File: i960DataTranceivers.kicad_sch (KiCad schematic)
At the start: 6 parts

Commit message: Update everything and keep laying out the i960 features
Use bus wires as much as possible
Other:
- company: (none) -> Joshua Scoggins
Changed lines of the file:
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@@
 (kicad_sch (version 20211123) (generator eeschema)
   (paper "A4")
+  (title_block
+    (date "2022-05-13")
+    (rev "1")
+    (company "Joshua Scoggins")
+  )
   (junction (at 122.936 25.146) (diameter 0) (color 0 0 0 0)
   )

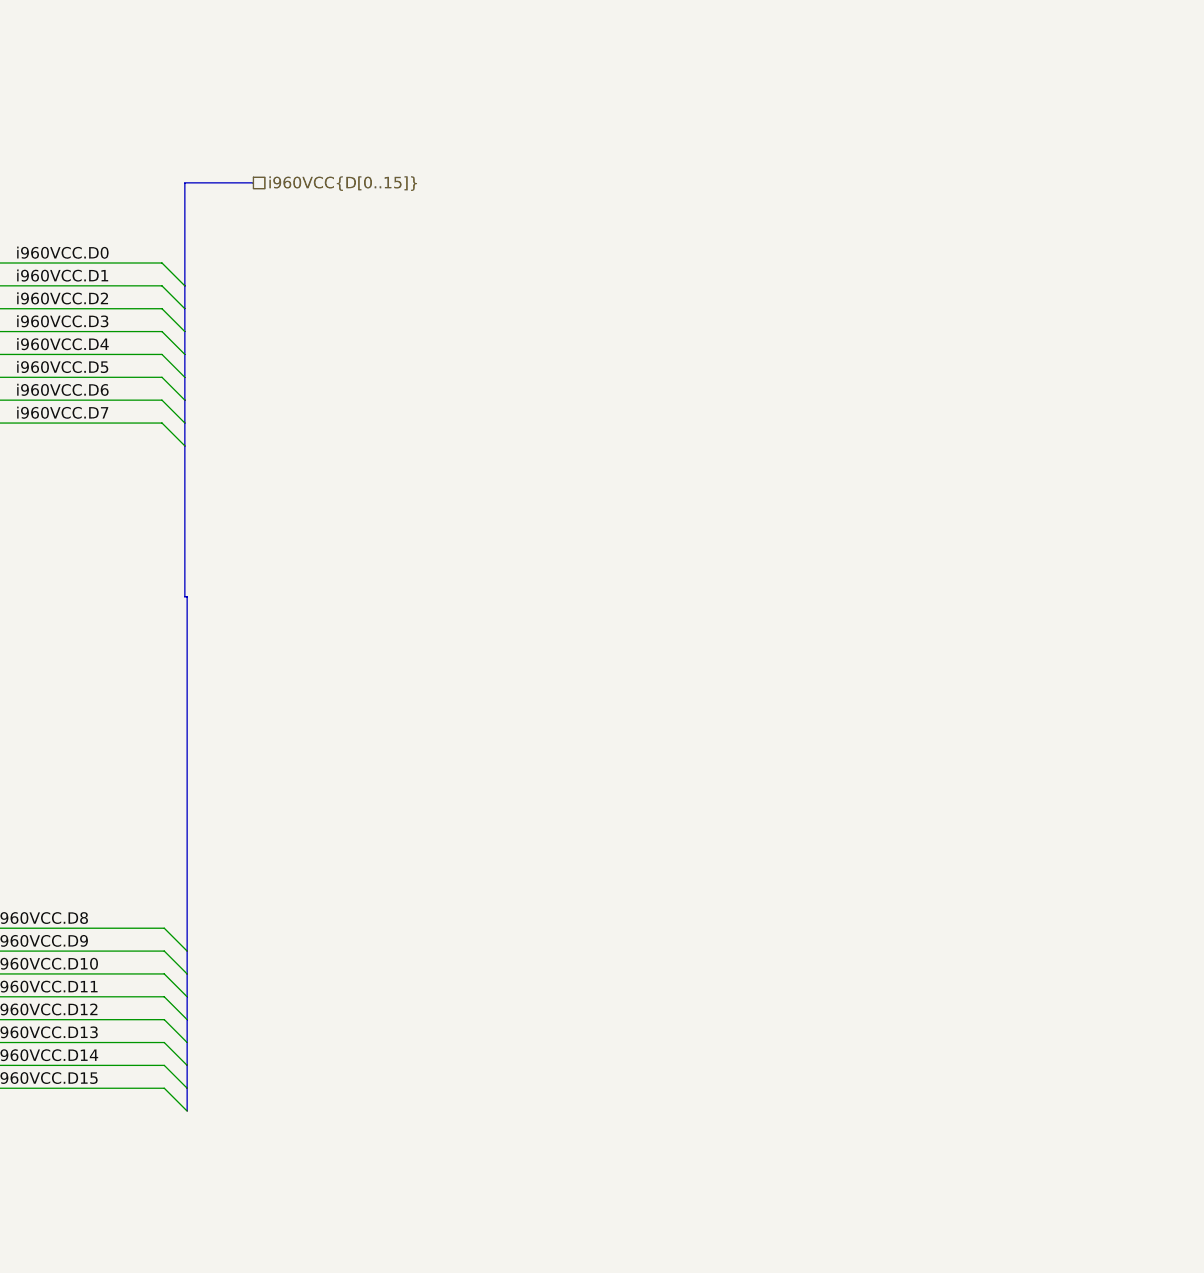
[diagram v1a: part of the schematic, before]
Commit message: Start defining the components needed for keeping track of the address and data lines
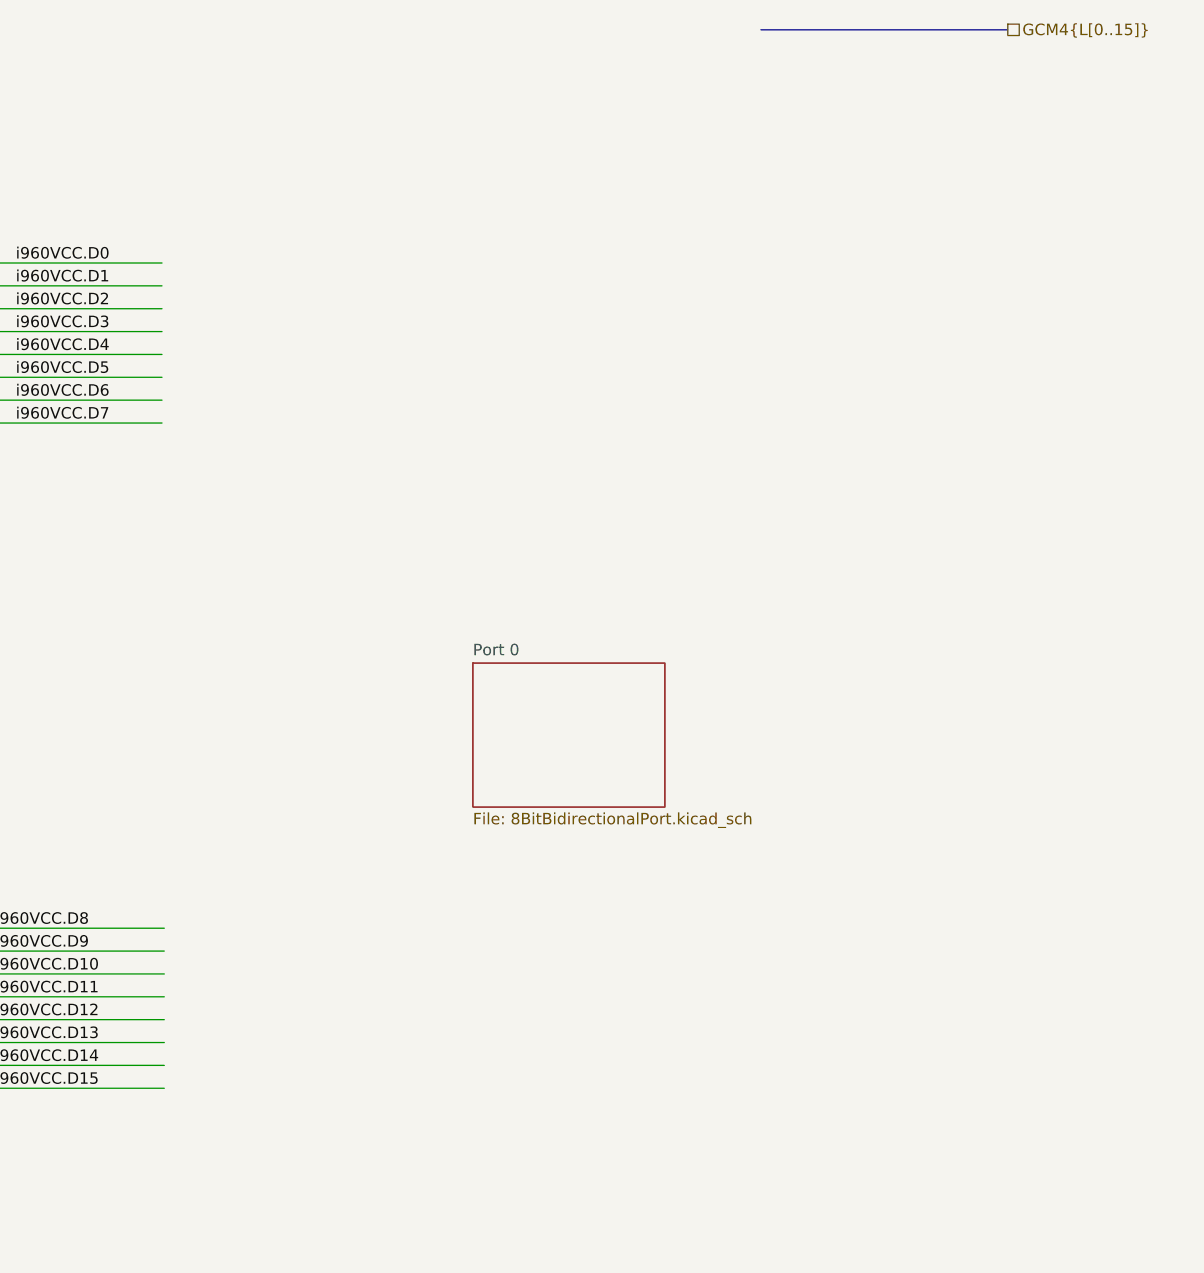
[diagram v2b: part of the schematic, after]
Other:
- added sheet Port 0 (8BitBidirectionalPort.kicad_sch)
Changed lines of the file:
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@@
   (junction (at 130.556 86.868) (diameter 0) (color 0 0 0 0)
   )
-  (bus_entry (at 168.148 126.492) (size 2.54 2.54)
-    (stroke (width 0) (type default) (color 0 0 0 0))
-  )
   (bus_entry (at 83.058 52.578) (size 2.54 2.54)
     (stroke (width 0) (type default) (color 0 0 0 0))
@@
     (stroke (width 0) (type default) (color 0 0 0 0))
   )
-  (bus_entry (at 167.894 60.198) (size 2.54 2.54)
-    (stroke (width 0) (type default) (color 0 0 0 0))
-  )
   (bus_entry (at 83.312 116.332) (size 2.54 2.54)
     (stroke (width 0) (type default) (color 0 0 0 0))
   )
-  (bus_entry (at 168.148 131.572) (size 2.54 2.54)
-    (stroke (width 0) (type default) (color 0 0 0 0))
-  )
   (bus_entry (at 83.312 121.412) (size 2.54 2.54)
     (stroke (width 0) (type default) (color 0 0 0 0))
@@
     (stroke (width 0) (type default) (color 0 0 0 0))
   )
-  (bus_entry (at 168.148 121.412) (size 2.54 2.54)
-    (stroke (width 0) (type default) (color 0 0 0 0))
-  )
-  (bus_entry (at 168.148 134.112) (size 2.54 2.54)
-    (stroke (width 0) (type default) (color 0 0 0 0))
-  )
-  (bus_entry (at 168.148 136.652) (size 2.54 2.54)
-    (stroke (width 0) (type default) (color 0 0 0 0))
-  )
   (bus_entry (at 83.058 42.418) (size 2.54 2.54)
     (stroke (width 0) (type default) (color 0 0 0 0))
   )
-  (bus_entry (at 167.894 57.658) (size 2.54 2.54)
-    (stroke (width 0) (type default) (color 0 0 0 0))
-  )
   (bus_entry (at 83.058 47.498) (size 2.54 2.54)
     (stroke (width 0) (type default) (color 0 0 0 0))
@@
     (stroke (width 0) (type default) (color 0 0 0 0))
   )
-  (bus_entry (at 167.894 62.738) (size 2.54 2.54)
-    (stroke (width 0) (type default) (color 0 0 0 0))
-  )
-  (bus_entry (at 167.894 52.578) (size 2.54 2.54)
-    (stroke (width 0) (type default) (color 0 0 0 0))
-  )
   (bus_entry (at 83.312 123.952) (size 2.54 2.54)
     (stroke (width 0) (type default) (color 0 0 0 0))
   )
-  (bus_entry (at 168.148 118.872) (size 2.54 2.54)
-    (stroke (width 0) (type default) (color 0 0 0 0))
-  )
   (bus_entry (at 83.058 65.278) (size 2.54 2.54)
     (stroke (width 0) (type default) (color 0 0 0 0))
@@
     (stroke (width 0) (type default) (color 0 0 0 0))
   )
-  (bus_entry (at 168.148 123.952) (size 2.54 2.54)
-    (stroke (width 0) (type default) (color 0 0 0 0))
-  )
   (bus_entry (at 83.058 60.198) (size 2.54 2.54)
     (stroke (width 0) (type default) (color 0 0 0 0))
@@
     (stroke (width 0) (type default) (color 0 0 0 0))
   )
-  (bus_entry (at 167.894 55.118) (size 2.54 2.54)
-    (stroke (width 0) (type default) (color 0 0 0 0))
-  )
-  (bus_entry (at 168.148 129.032) (size 2.54 2.54)
-    (stroke (width 0) (type default) (color 0 0 0 0))
-  )
-  (bus_entry (at 167.894 44.958) (size 2.54 2.54)
-    (stroke (width 0) (type default) (color 0 0 0 0))
-  )
-  (bus_entry (at 167.894 47.498) (size 2.54 2.54)
-    (stroke (width 0) (type default) (color 0 0 0 0))
-  )
-  (bus_entry (at 167.894 50.038) (size 2.54 2.54)
-    (stroke (width 0) (type default) (color 0 0 0 0))
-  )
   (bus_entry (at 83.058 44.958) (size 2.54 2.54)
     (stroke (width 0) (type default) (color 0 0 0 0))
@@
     (stroke (width 0) (type default) (color 0 0 0 0))
   )
-  (bus (pts (xy 170.434 62.738) (xy 170.434 60.198))
-    (stroke (width 0) (type default) (color 0 0 0 0))
-  )
-  (bus (pts (xy 170.688 121.412) (xy 170.688 82.042))
-    (stroke (width 0) (type default) (color 0 0 0 0))
-  )
   (bus (pts (xy 83.058 50.038) (xy 83.058 52.578))
     (stroke (width 0) (type default) (color 0 0 0 0))
   )
-  (bus (pts (xy 170.688 123.952) (xy 170.688 121.412))
-    (stroke (width 0) (type default) (color 0 0 0 0))
-  )
   (wire (pts (xy 141.732 160.782) (xy 130.81 160.782))
     (stroke (width 0) (type default) (color 0 0 0 0))
@@
     (stroke (width 0) (type default) (color 0 0 0 0))
   )
-  (bus (pts (xy 170.434 52.578) (xy 170.434 50.038))
-    (stroke (width 0) (type default) (color 0 0 0 0))
-  )
   (wire (pts (xy 85.598 55.118) (xy 116.586 55.118))
     (stroke (width 0) (type default) (color 0 0 0 0))
@@
     (stroke (width 0) (type default) (color 0 0 0 0))
   )
-  (bus (pts (xy 170.434 50.038) (xy 170.434 47.498))
-    (stroke (width 0) (type default) (color 0 0 0 0))
-  )
-  (bus (pts (xy 170.434 57.658) (xy 170.434 55.118))
-    (stroke (width 0) (type default) (color 0 0 0 0))
-  )
   (wire (pts (xy 130.556 86.868) (xy 130.556 80.518))
     (stroke (width 0) (type default) (color 0 0 0 0))
@@
     (stroke (width 0) (type default) (color 0 0 0 0))
   )
-  (bus (pts (xy 170.434 65.278) (xy 170.434 82.042))
-    (stroke (width 0) (type default) (color 0 0 0 0))
-  )
   (bus (pts (xy 83.058 47.498) (xy 83.058 50.038))
     (stroke (width 0) (type default) (color 0 0 0 0))
@@
     (stroke (width 0) (type default) (color 0 0 0 0))
   )
-  (bus (pts (xy 170.434 65.278) (xy 170.434 62.738))
-    (stroke (width 0) (type default) (color 0 0 0 0))
-  )
   (wire (pts (xy 85.598 60.198) (xy 116.586 60.198))
     (stroke (width 0) (type default) (color 0 0 0 0))
@@
     (stroke (width 0) (type default) (color 0 0 0 0))
   )
+  (bus (pts (xy 234.442 19.05) (xy 261.874 19.05))
+    (stroke (width 0) (type default) (color 0 0 0 0))
+  )
   (wire (pts (xy 136.906 60.198) (xy 167.894 60.198))
     (stroke (width 0) (type default) (color 0 0 0 0))
@@
     (stroke (width 0) (type default) (color 0 0 0 0))
   )
-  (bus (pts (xy 170.434 55.118) (xy 170.434 52.578))
-    (stroke (width 0) (type default) (color 0 0 0 0))
-  )
   (wire (pts (xy 107.442 70.358) (xy 116.586 70.358))
     (stroke (width 0) (type default) (color 0 0 0 0))
@@
     (stroke (width 0) (type default) (color 0 0 0 0))
   )
-  (bus (pts (xy 170.688 129.032) (xy 170.688 126.492))
-    (stroke (width 0) (type default) (color 0 0 0 0))
-  )
   (wire (pts (xy 136.906 50.038) (xy 167.894 50.038))
     (stroke (width 0) (type default) (color 0 0 0 0))
   )
-  (bus (pts (xy 170.688 136.652) (xy 170.688 134.112))
-    (stroke (width 0) (type default) (color 0 0 0 0))
-  )
   (wire (pts (xy 111.506 25.146) (xy 122.936 25.146))
     (stroke (width 0) (type default) (color 0 0 0 0))
@@
     (stroke (width 0) (type default) (color 0 0 0 0))
   )
-  (bus (pts (xy 170.688 82.042) (xy 170.434 82.042))
-    (stroke (width 0) (type default) (color 0 0 0 0))
-  )
   (wire (pts (xy 85.598 52.578) (xy 116.586 52.578))
     (stroke (width 0) (type default) (color 0 0 0 0))
@@
     (stroke (width 0) (type default) (color 0 0 0 0))
   )
-  (bus (pts (xy 170.434 60.198) (xy 170.434 57.658))
-    (stroke (width 0) (type default) (color 0 0 0 0))
-  )
   (wire (pts (xy 104.14 67.818) (xy 104.14 141.732))
     (stroke (width 0) (type default) (color 0 0 0 0))
@@
     (stroke (width 0) (type default) (color 0 0 0 0))
   )
-  (bus (pts (xy 170.434 36.068) (xy 178.054 36.068))
-    (stroke (width 0) (type default) (color 0 0 0 0))
-  )
   (wire (pts (xy 85.852 123.952) (xy 116.84 123.952))
     (stroke (width 0) (type default) (color 0 0 0 0))
@@
     (stroke (width 0) (type default) (color 0 0 0 0))
   )
-  (bus (pts (xy 170.688 131.572) (xy 170.688 129.032))
-    (stroke (width 0) (type default) (color 0 0 0 0))
-  )
   (wire (pts (xy 136.906 62.738) (xy 167.894 62.738))
     (stroke (width 0) (type default) (color 0 0 0 0))
   )
-  (bus (pts (xy 170.688 134.112) (xy 170.688 131.572))
-    (stroke (width 0) (type default) (color 0 0 0 0))
-  )
   (wire (pts (xy 137.16 131.572) (xy 168.148 131.572))
     (stroke (width 0) (type default) (color 0 0 0 0))
@@
     (stroke (width 0) (type default) (color 0 0 0 0))
   )
-  (bus (pts (xy 170.688 126.492) (xy 170.688 123.952))
-    (stroke (width 0) (type default) (color 0 0 0 0))
-  )
   (wire (pts (xy 123.19 160.782) (xy 111.76 160.782))
     (stroke (width 0) (type default) (color 0 0 0 0))
   )
-  (bus (pts (xy 170.434 47.498) (xy 170.434 36.068))
-    (stroke (width 0) (type default) (color 0 0 0 0))
-  )
   (wire (pts (xy 85.598 44.958) (xy 116.586 44.958))
     (stroke (width 0) (type default) (color 0 0 0 0))
   )
-  (bus (pts (xy 170.688 139.192) (xy 170.688 136.652))
-    (stroke (width 0) (type default) (color 0 0 0 0))
-  )
   (wire (pts (xy 85.852 129.032) (xy 116.84 129.032))
     (stroke (width 0) (type default) (color 0 0 0 0))
@@
     (effects (font (size 1.27 1.27)) (justify left bottom))
   )
-  (hierarchical_label "i960VCC{D[0..15]}" (shape passive) (at 178.054 36.068 0)
+  (hierarchical_label "GCM4{L[0..15]}" (shape passive) (at 261.874 19.05 0)
     (effects (font (size 1.27 1.27)) (justify left))
   )
@@
     (pin "1")
   )
+  (sheet (at 202.438 89.408) (size 21.336 16.002) (fields_autoplaced)
+    (stroke (width 0.1524) (type solid) (color 0 0 0 0))
+    (fill (color 0 0 0 0.0000))
+    (property "Sheet name" "Port 0" (id 0) (at 202.438 88.6964 0)
+      (effects (font (size 1.27 1.27)) (justify left bottom))
+    )
+    (property "Sheet file" "8BitBidirectionalPort.kicad_sch" (id 1) (at 202.438 105.9946 0)
+      (effects (font (size 1.27 1.27)) (justify left top))
+    )
+  )
 )

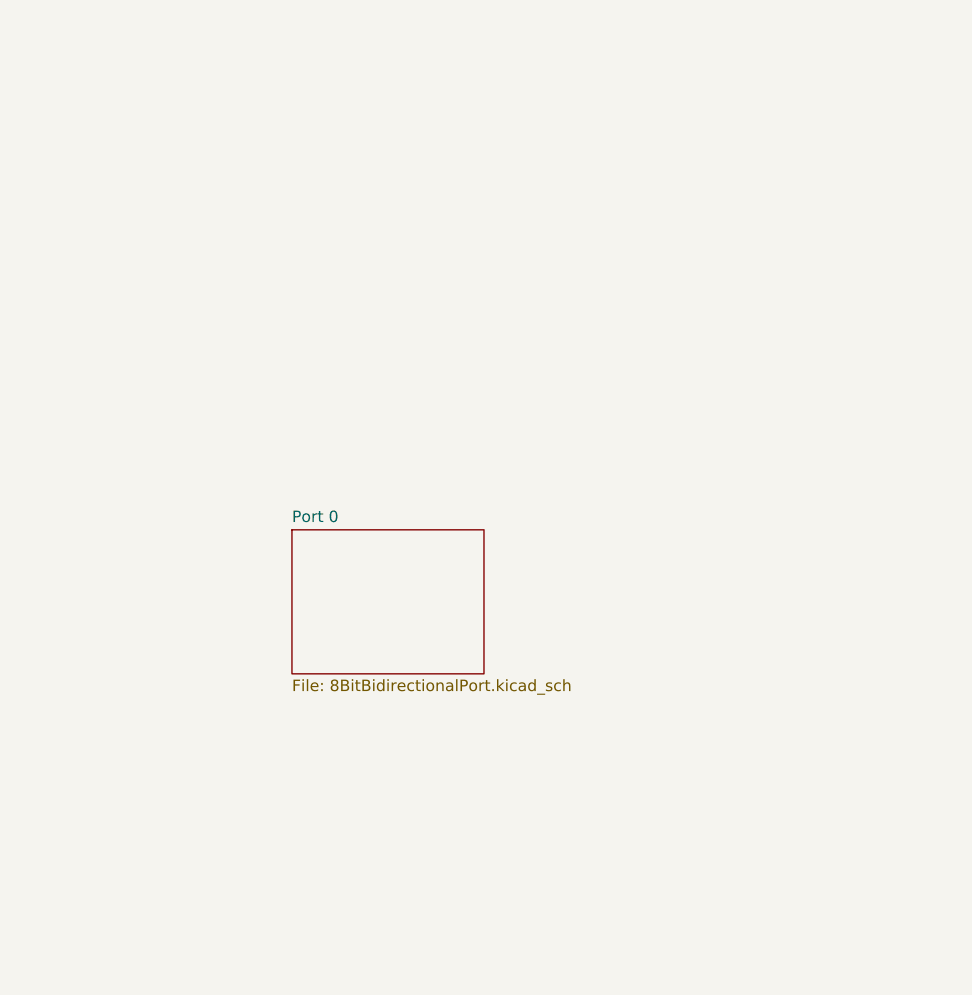
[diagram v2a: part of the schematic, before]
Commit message: Added a 16-bit transceiver to data lines
There is no latch in this design, the GCM4 is responsible for keeping
the lines active when handling read requests from the i960. This isn't
that big of a deal. It just means that we have to keep the data line id
set for as long as possible.

This is basically what I do now for the gcm4 based boards just without
the address bits set. The data lines stay set until the next time they
need to be modified.
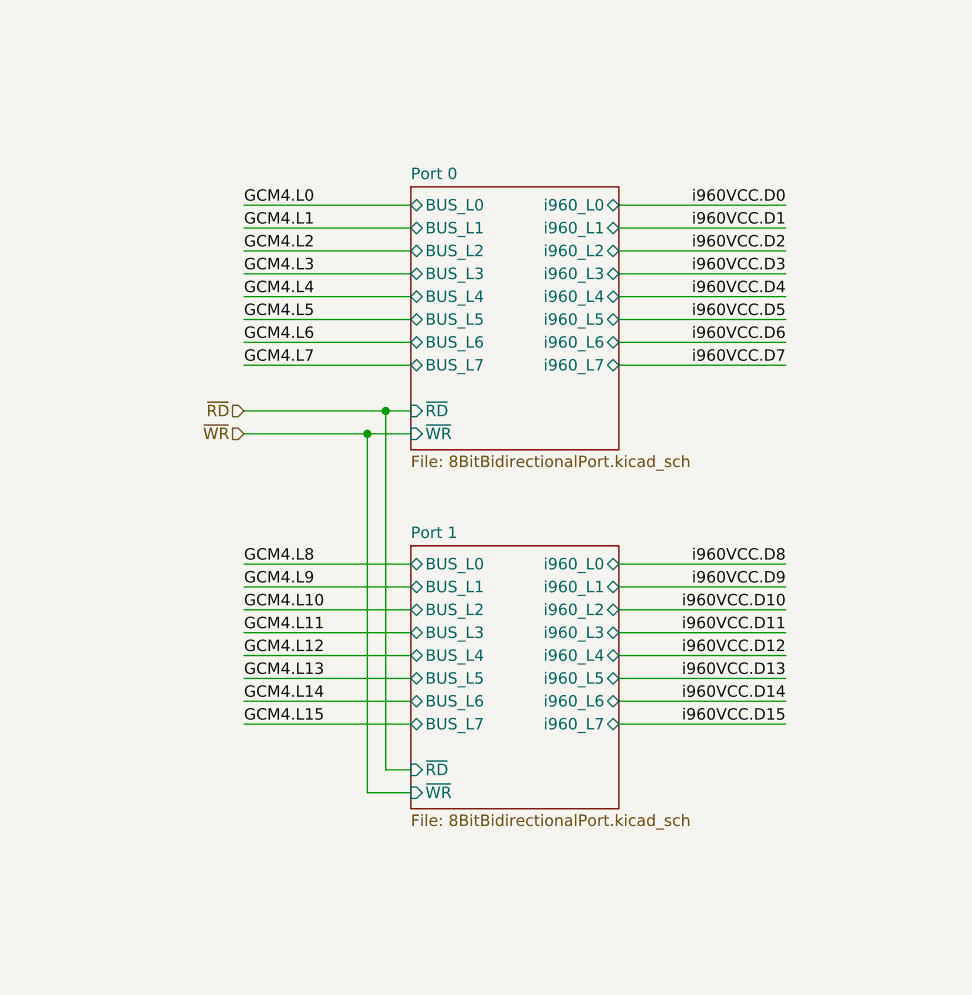
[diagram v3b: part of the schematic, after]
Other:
- added sheet Port 1 (8BitBidirectionalPort.kicad_sch)
- sheet Port 0 ports: added BUS_L0, BUS_L1, BUS_L2, BUS_L3, BUS_L4, BUS_L5, BUS_L6, BUS_L7, i960_L0, i960_L1, i960_L2, i960_L3, i960_L4, i960_L5, i960_L6, i960_L7, ~{RD}, ~{WR}; removed none
